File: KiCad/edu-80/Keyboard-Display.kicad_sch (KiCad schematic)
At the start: 69 parts, among them Q10 ED1602, Q11 ED1602, Q12 ED1602, Q13 ED1602, Q14 ED1602, Q15 ED1602, Q16 ED1602, Q17 ED1602, Q18 ED1602, Q19 ED1602, Q20 ED1602, Q4 ED1602, Q5 ED1602, Q6 ED1602, Q7 ED1602, Q8 ED1602, Q9 ED1602, U21 7442

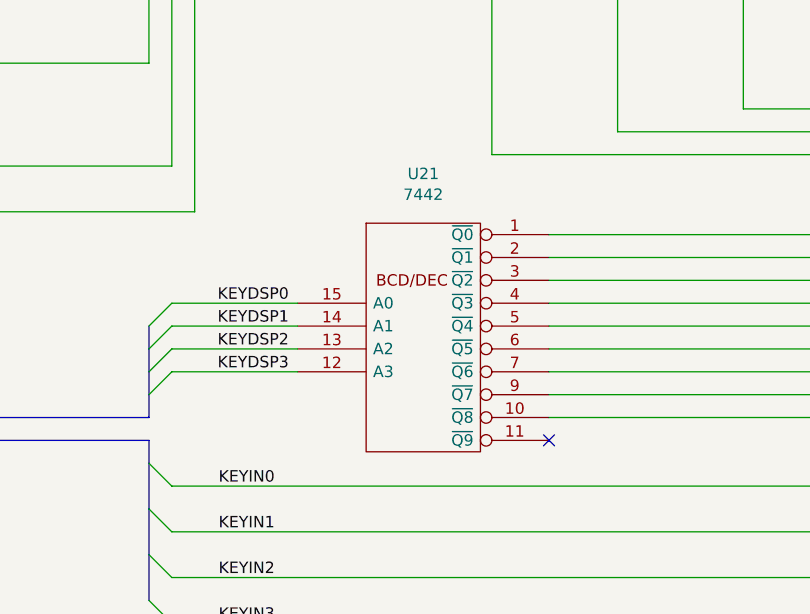
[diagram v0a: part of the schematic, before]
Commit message: Fixed lst of the errors, still two warnings
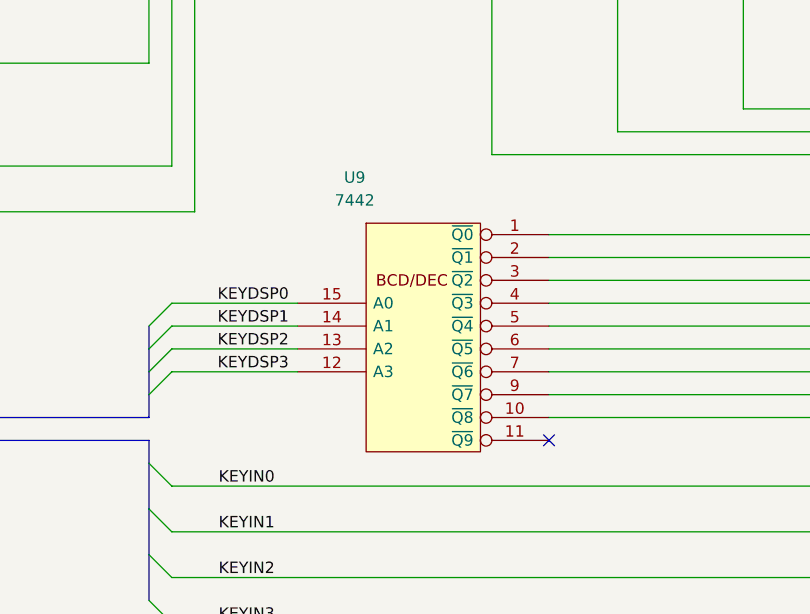
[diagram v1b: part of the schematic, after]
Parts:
- removed U21: 7442, symbol edu-80-rescue:7442-74xx_IEEE
- added U9: 7442, symbol Edu-80_Symbols:7442
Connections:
- net GND: now also U9.8 (GND)
- net KEYDSP0: now also U9.15 (A0)
- net KEYDSP1: now also U9.14 (A1)
- net KEYDSP2: now also U9.13 (A2)
- net KEYDSP3: now also U9.12 (A3)
- net VCC: now also U9.16 (VCC)
- net at CP50.2 (Y1), CP50.4 (Y2), CP51.2 (Y1)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: now also U9.6 (~{Q5})
- net at CP60.2 (Y1), CP60.4 (Y2), CP61.2 (Y1)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: now also U9.7 (~{Q6})
- net at CP70.2 (Y1), CP70.4 (Y2), CP71.2 (Y1)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: now also U9.9 (~{Q7})
- net at Q20.2 (B): now also U9.10 (~{Q8})
- net at CP0.2 (Y1), CP0.4 (Y2), CP02.2 (Y1)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: now also U9.1 (~{Q0})
- net at CP10.2 (Y1), CP10.4 (Y2), CP11.2 (Y1)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: now also U9.2 (~{Q1})
- net at CP20.2 (Y1), CP20.4 (Y2), CP21.2 (Y1)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: now also U9.3 (~{Q2})
- net at CP30.1 (X1), CP30.3 (X3), CP31.2 (Y1)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: now also U9.4 (~{Q3})
- net at CP40.2 (Y1), CP40.4 (Y2), CP41.2 (Y1)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: now also U9.5 (~{Q4})
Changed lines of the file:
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@@
-    )
-  )
-  (symbol (lib_id "edu-80-rescue:7442-74xx_IEEE") (at 116.84 123.19 0) (unit 1)
-    (in_bom yes) (on_board yes) (dnp no)
-    (property "Reference" "U21" (at 116.84 105.0036 0)
-      (effects (font (size 1.27 1.27)))
-    )
-    (property "Value" "7442" (at 116.84 107.315 0)
-      (effects (font (size 1.27 1.27)))
-    )
-    (property "Footprint" "" (at 116.84 123.19 0)
-      (effects (font (size 1.27 1.27)) hide)
-    )
-    (property "Datasheet" "" (at 116.84 123.19 0)
-      (effects (font (size 1.27 1.27)) hide)
-    )
-    (pin "16")
-    (pin "8")
-    (pin "1")
-    (pin "10")
-    (pin "11")
-    (pin "12")
-    (pin "13")
-    (pin "14")
-    (pin "15")
-    (pin "2")
-    (pin "3")
-    (pin "4")
-    (pin "5")
-    (pin "6")
-    (pin "7")
-    (pin "9")
-    (instances
-      (project "edu-80"
-        (path "/d19d6db6-a96a-43e3-aa50-c057821f7e22"
-          (reference "U21") (unit 1)
-        )
-        (path "/d19d6db6-a96a-43e3-aa50-c057821f7e22/00000000-0000-0000-0000-000063e4dc54"
-          (reference "U21") (unit 1)
-        )
-      )
     )
   )
@@
         )
       )
+    )
+  )
+  (symbol (lib_id "Edu-80_Symbols:7442") (at 116.84 123.19 0) (unit 1)
+    (in_bom yes) (on_board yes) (dnp no)
+    (property "Reference" "U9" (at 109.22 105.41 0)
+      (effects (font (size 1.27 1.27)))
+    )
+    (property "Value" "7442" (at 109.22 107.95 0)
+      (effects (font (size 1.27 1.27)))
+    )
+    (property "Footprint" "" (at 116.84 123.19 0)
+      (effects (font (size 1.27 1.27)) hide)
+    )
+    (property "Datasheet" "" (at 116.84 123.19 0)
+      (effects (font (size 1.27 1.27)) hide)
+    )
+    (pin "16")
+    (pin "8")
+    (pin "1")
+    (pin "10")
+    (pin "11")
+    (pin "12")
+    (pin "13")
+    (pin "14")
+    (pin "15")
+    (pin "2")
+    (pin "3")
+    (pin "4")
+    (pin "5")
+    (pin "6")
+    (pin "7")
+    (pin "9")
+    (instances
+      (project "edu-80"
+        (path "/d19d6db6-a96a-43e3-aa50-c057821f7e22/00000000-0000-0000-0000-000063e35f90"
+          (reference "U9") (unit 1)
+        )
+        (path "/d19d6db6-a96a-43e3-aa50-c057821f7e22/00000000-0000-0000-0000-000063e4dc54"
+          (reference "U21") (unit 1)
+        )
+      )

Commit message: Working on removing edu-80-rescue symbol library
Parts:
- removed CP80: RS, symbol edu-80-rescue:key_crosspoint-Edu-80_Symbol
- removed CP81: CK, symbol edu-80-rescue:key_crosspoint-Edu-80_Symbol
- removed CP82: K1, symbol edu-80-rescue:key_crosspoint-Edu-80_Symbol
- removed CP83: K2, symbol edu-80-rescue:key_crosspoint-Edu-80_Symbol
- removed CP84: K3, symbol edu-80-rescue:key_crosspoint-Edu-80_Symbol
- removed CP85: K4, symbol edu-80-rescue:key_crosspoint-Edu-80_Symbol
- added CP4: RS, symbol Edu-80_Symbols:key_crosspoint
- added CP5: CK, symbol Edu-80_Symbols:key_crosspoint
- added CP6: K1, symbol Edu-80_Symbols:key_crosspoint
- added CP7: K2, symbol Edu-80_Symbols:key_crosspoint
- added CP8: K3, symbol Edu-80_Symbols:key_crosspoint
- added CP9: K4, symbol Edu-80_Symbols:key_crosspoint
- CP0, CP02, CP03, CP1, CP10, CP20: symbol edu-80-rescue:key_crosspoint-Edu-80_Symbol -> Edu-80_Symbols:key_crosspoint
- DSP1: symbol edu-80-rescue:Edu-80_Display-Edu-80_Symbol -> Edu-80_Symbols:Edu-80_Display
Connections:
- net CKKEY: now also CP5.1 (X1), CP5.3 (X2)
- net Earth: now also CP4.2 (Y1), CP4.4 (Y2), CP5.2 (Y1), CP5.4 (Y2), CP6.2 (Y1), CP6.4 (Y2), CP7.2 (Y1), CP7.4 (Y2), CP8.2 (Y1), CP8.4 (Y2), CP9.2 (Y1), CP9.4 (Y2)
- net K1: now also CP6.1 (X1), CP6.3 (X2)
- net K2: now also CP7.1 (X1), CP7.3 (X2)
- net K3: now also CP8.1 (X1), CP8.3 (X2)
- net K4: now also CP9.1 (X1), CP9.3 (X2)
- net ~{RST}: now also CP4.1 (X1), CP4.3 (X2)

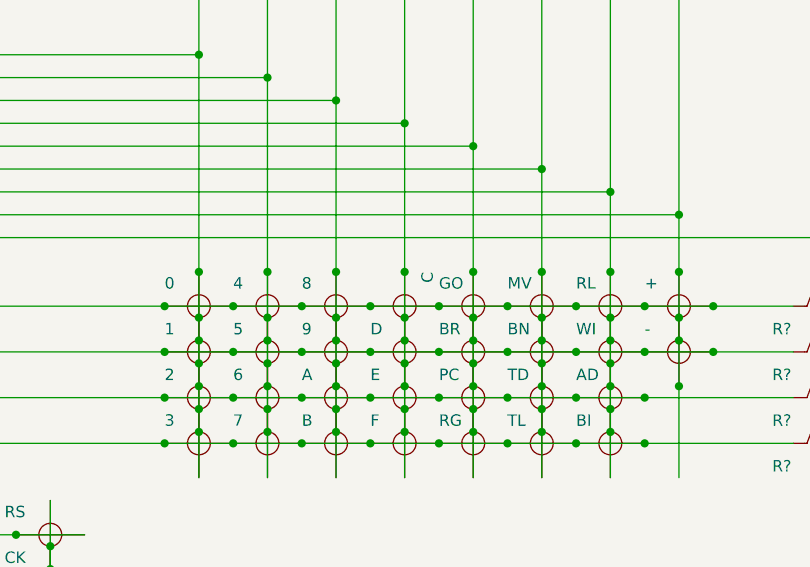
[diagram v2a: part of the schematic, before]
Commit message: Cleaning up the PAL-003 decoding, adding Modifications page.
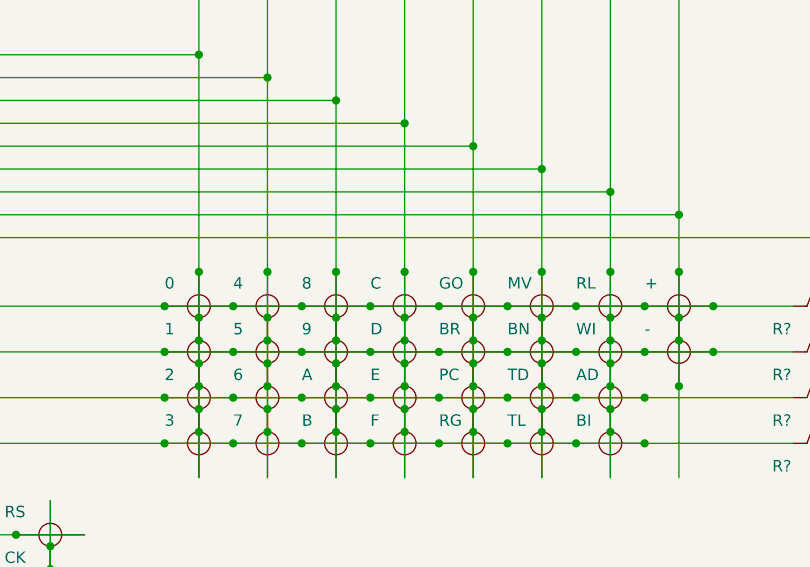
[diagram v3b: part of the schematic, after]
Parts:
- CP11, CP12, CP13, CP21, CP22, CP23, CP30, CP31, CP32, CP33, CP40, CP41, CP42, CP43, CP50, CP51, CP52, CP53, CP60, CP61, CP62, CP63: symbol edu-80-rescue:key_crosspoint-Edu-80_Symbol -> Edu-80_Symbols:key_crosspoint
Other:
- company: (none) -> Strangers
- title: (none) -> Edu-80 Z80 Trainer
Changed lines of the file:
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@@
 (kicad_sch (version 20230121) (generator eeschema)
   (paper "A")
+  (title_block
+    (title "Edu-80 Z80 Trainer")
+    (date "2023-06-03")
+    (rev "0.1")
+    (company "Strangers")
+    (comment 1 "Author: James D. Tucker")
+  )
   (junction (at 187.96 85.09) (diameter 0) (color 0 0 0 0)
   )
@@
     )
   )
-  (symbol (lib_id "edu-80-rescue:key_crosspoint-Edu-80_Symbol") (at 173.99 144.78 0) (unit 1)
+  (symbol (lib_name "key_crosspoint_14") (lib_id "Edu-80_Symbols:key_crosspoint") (at 173.99 144.78 0) (unit 1)
     (in_bom yes) (on_board yes) (dnp no)
     (property "Reference" "CP11" (at 171.45 144.78 0)
@@
     )
   )
-  (symbol (lib_id "edu-80-rescue:key_crosspoint-Edu-80_Symbol") (at 173.99 149.86 0) (unit 1)
+  (symbol (lib_name "key_crosspoint_15") (lib_id "Edu-80_Symbols:key_crosspoint") (at 173.99 149.86 0) (unit 1)
     (in_bom yes) (on_board yes) (dnp no)
     (property "Reference" "CP12" (at 171.45 149.86 0)
@@
     )
   )
-  (symbol (lib_id "edu-80-rescue:key_crosspoint-Edu-80_Symbol") (at 173.99 154.94 0) (unit 1)
+  (symbol (lib_name "key_crosspoint_16") (lib_id "Edu-80_Symbols:key_crosspoint") (at 173.99 154.94 0) (unit 1)
     (in_bom yes) (on_board yes) (dnp no)
     (property "Reference" "CP13" (at 171.45 154.94 0)
@@
     )
   )
-  (symbol (lib_id "edu-80-rescue:key_crosspoint-Edu-80_Symbol") (at 181.61 144.78 0) (unit 1)
+  (symbol (lib_name "key_crosspoint_17") (lib_id "Edu-80_Symbols:key_crosspoint") (at 181.61 144.78 0) (unit 1)
     (in_bom yes) (on_board yes) (dnp no)
     (property "Reference" "CP21" (at 179.07 144.78 0)
@@
     )
   )
-  (symbol (lib_id "edu-80-rescue:key_crosspoint-Edu-80_Symbol") (at 181.61 149.86 0) (unit 1)
+  (symbol (lib_name "key_crosspoint_18") (lib_id "Edu-80_Symbols:key_crosspoint") (at 181.61 149.86 0) (unit 1)
     (in_bom yes) (on_board yes) (dnp no)
     (property "Reference" "CP22" (at 179.07 149.86 0)
@@
     )
   )
-  (symbol (lib_id "edu-80-rescue:key_crosspoint-Edu-80_Symbol") (at 181.61 154.94 0) (unit 1)
+  (symbol (lib_name "key_crosspoint_19") (lib_id "Edu-80_Symbols:key_crosspoint") (at 181.61 154.94 0) (unit 1)
     (in_bom yes) (on_board yes) (dnp no)
     (property "Reference" "CP23" (at 179.07 154.94 0)
@@
     )
   )
-  (symbol (lib_id "edu-80-rescue:key_crosspoint-Edu-80_Symbol") (at 189.23 139.7 270) (unit 1)
+  (symbol (lib_name "key_crosspoint_20") (lib_id "Edu-80_Symbols:key_crosspoint") (at 189.23 139.7 270) (unit 1)
     (in_bom yes) (on_board yes) (dnp no)
     (property "Reference" "CP30" (at 189.23 137.16 0)
       (effects (font (size 1.27 1.27)) (justify left) hide)
     )
-    (property "Value" "C" (at 191.77 135.89 0)
+    (property "Value" "C" (at 185.42 137.16 90)
       (effects (font (size 1.27 1.27)) (justify left))
     )
@@
     )
   )
-  (symbol (lib_id "edu-80-rescue:key_crosspoint-Edu-80_Symbol") (at 189.23 144.78 0) (unit 1)
+  (symbol (lib_name "key_crosspoint_21") (lib_id "Edu-80_Symbols:key_crosspoint") (at 189.23 144.78 0) (unit 1)
     (in_bom yes) (on_board yes) (dnp no)
     (property "Reference" "CP31" (at 186.69 144.78 0)
@@
     )
   )
-  (symbol (lib_id "edu-80-rescue:key_crosspoint-Edu-80_Symbol") (at 189.23 149.86 0) (unit 1)
+  (symbol (lib_name "key_crosspoint_22") (lib_id "Edu-80_Symbols:key_crosspoint") (at 189.23 149.86 0) (unit 1)
     (in_bom yes) (on_board yes) (dnp no)
     (property "Reference" "CP32" (at 186.69 149.86 0)
@@
     )
   )
-  (symbol (lib_id "edu-80-rescue:key_crosspoint-Edu-80_Symbol") (at 189.23 154.94 0) (unit 1)
+  (symbol (lib_name "key_crosspoint_23") (lib_id "Edu-80_Symbols:key_crosspoint") (at 189.23 154.94 0) (unit 1)
     (in_bom yes) (on_board yes) (dnp no)
     (property "Reference" "CP33" (at 186.69 154.94 0)
@@
     )
   )
-  (symbol (lib_id "edu-80-rescue:key_crosspoint-Edu-80_Symbol") (at 196.85 139.7 0) (unit 1)
+  (symbol (lib_name "key_crosspoint_24") (lib_id "Edu-80_Symbols:key_crosspoint") (at 196.85 139.7 0) (unit 1)
     (in_bom yes) (on_board yes) (dnp no)
     (property "Reference" "CP40" (at 194.31 139.7 0)
@@
     )
   )
-  (symbol (lib_id "edu-80-rescue:key_crosspoint-Edu-80_Symbol") (at 196.85 144.78 0) (unit 1)
+  (symbol (lib_name "key_crosspoint_25") (lib_id "Edu-80_Symbols:key_crosspoint") (at 196.85 144.78 0) (unit 1)
     (in_bom yes) (on_board yes) (dnp no)
     (property "Reference" "CP41" (at 194.31 144.78 0)
@@
     )
   )
-  (symbol (lib_id "edu-80-rescue:key_crosspoint-Edu-80_Symbol") (at 196.85 149.86 0) (unit 1)
+  (symbol (lib_name "key_crosspoint_26") (lib_id "Edu-80_Symbols:key_crosspoint") (at 196.85 149.86 0) (unit 1)
     (in_bom yes) (on_board yes) (dnp no)
     (property "Reference" "CP42" (at 194.31 149.86 0)
@@
     )
   )
-  (symbol (lib_id "edu-80-rescue:key_crosspoint-Edu-80_Symbol") (at 196.85 154.94 0) (unit 1)
+  (symbol (lib_name "key_crosspoint_27") (lib_id "Edu-80_Symbols:key_crosspoint") (at 196.85 154.94 0) (unit 1)
     (in_bom yes) (on_board yes) (dnp no)
     (property "Reference" "CP43" (at 194.31 154.94 0)
@@
     )
   )
-  (symbol (lib_id "edu-80-rescue:key_crosspoint-Edu-80_Symbol") (at 204.47 139.7 0) (unit 1)
+  (symbol (lib_name "key_crosspoint_28") (lib_id "Edu-80_Symbols:key_crosspoint") (at 204.47 139.7 0) (unit 1)
     (in_bom yes) (on_board yes) (dnp no)
     (property "Reference" "CP50" (at 201.93 139.7 0)
@@
     )
   )
-  (symbol (lib_id "edu-80-rescue:key_crosspoint-Edu-80_Symbol") (at 204.47 144.78 0) (unit 1)
+  (symbol (lib_name "key_crosspoint_29") (lib_id "Edu-80_Symbols:key_crosspoint") (at 204.47 144.78 0) (unit 1)
     (in_bom yes) (on_board yes) (dnp no)
     (property "Reference" "CP51" (at 201.93 144.78 0)
@@
     )
   )
-  (symbol (lib_id "edu-80-rescue:key_crosspoint-Edu-80_Symbol") (at 204.47 149.86 0) (unit 1)
+  (symbol (lib_name "key_crosspoint_30") (lib_id "Edu-80_Symbols:key_crosspoint") (at 204.47 149.86 0) (unit 1)
     (in_bom yes) (on_board yes) (dnp no)
     (property "Reference" "CP52" (at 201.93 149.86 0)
@@
     )
   )
-  (symbol (lib_id "edu-80-rescue:key_crosspoint-Edu-80_Symbol") (at 204.47 154.94 0) (unit 1)
+  (symbol (lib_name "key_crosspoint_31") (lib_id "Edu-80_Symbols:key_crosspoint") (at 204.47 154.94 0) (unit 1)
     (in_bom yes) (on_board yes) (dnp no)
     (property "Reference" "CP53" (at 201.93 154.94 0)
@@
     )
   )
-  (symbol (lib_id "edu-80-rescue:key_crosspoint-Edu-80_Symbol") (at 212.09 139.7 0) (unit 1)
+  (symbol (lib_name "key_crosspoint_32") (lib_id "Edu-80_Symbols:key_crosspoint") (at 212.09 139.7 0) (unit 1)
     (in_bom yes) (on_board yes) (dnp no)
     (property "Reference" "CP60" (at 209.55 139.7 0)
@@
     )
   )
-  (symbol (lib_id "edu-80-rescue:key_crosspoint-Edu-80_Symbol") (at 212.09 144.78 0) (unit 1)
+  (symbol (lib_name "key_crosspoint_33") (lib_id "Edu-80_Symbols:key_crosspoint") (at 212.09 144.78 0) (unit 1)
     (in_bom yes) (on_board yes) (dnp no)
     (property "Reference" "CP61" (at 209.55 144.78 0)
@@
     )
   )
-  (symbol (lib_id "edu-80-rescue:key_crosspoint-Edu-80_Symbol") (at 212.09 149.86 0) (unit 1)
+  (symbol (lib_name "key_crosspoint_34") (lib_id "Edu-80_Symbols:key_crosspoint") (at 212.09 149.86 0) (unit 1)
     (in_bom yes) (on_board yes) (dnp no)
     (property "Reference" "CP62" (at 209.55 149.86 0)
@@
     )
   )
-  (symbol (lib_id "edu-80-rescue:key_crosspoint-Edu-80_Symbol") (at 212.09 154.94 0) (unit 1)
+  (symbol (lib_name "key_crosspoint_35") (lib_id "Edu-80_Symbols:key_crosspoint") (at 212.09 154.94 0) (unit 1)
     (in_bom yes) (on_board yes) (dnp no)
     (property "Reference" "CP63" (at 209.55 154.94 0)
